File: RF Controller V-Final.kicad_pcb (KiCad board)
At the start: 2 copper layers, 132 x 67.5 mm, 37 parts, among them J3 BAT+, J4 BAT-, SW1 EG1218, U1 Teensy4.0, U7 Pitch/Roll, U9 Throttle/Yaw

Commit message: Modified traces
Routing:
- net /CSN: track 62.1 -> 62.7 mm
- net /MOSI: vias 2 -> 3
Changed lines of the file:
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@@
 	)
 	(segment
-		(start 136.82 102.18)
-		(end 114.03 102.18)
+		(start 136 103)
+		(end 114.85 103)
 		(width 0.2)
 		(layer "F.Cu")
@@
 	)
 	(segment
+		(start 114.85 103)
+		(end 112.93 101.08)
+		(width 0.2)
+		(layer "F.Cu")
+		(net "/CSN")
+	)
+	(segment
 		(start 138.5 100.5)
-		(end 136.82 102.18)
-		(width 0.2)
-		(layer "F.Cu")
-		(net "/CSN")
-	)
-	(segment
-		(start 114.03 102.18)
-		(end 112.93 101.08)
+		(end 136 103)
 		(width 0.2)
 		(layer "F.Cu")
@@
 	)
 	(segment
+		(start 135.5 102.4)
+		(end 116.79 102.4)
+		(width 0.2)
+		(layer "F.Cu")
+		(net "/MOSI")
+	)
+	(segment
 		(start 158.5 81.5)
 		(end 156.5 81.5)
@@
 		(net "/MOSI")
 	)
+	(segment
+		(start 116.79 102.4)
+		(end 115.47 101.08)
+		(width 0.2)
+		(layer "F.Cu")
+		(net "/MOSI")
+	)
 	(via
 		(at 158.534265 81.534265)
+		(size 0.6)
+		(drill 0.3)
+		(layers "F.Cu" "B.Cu")
+		(net "/MOSI")
+	)
+	(via
+		(at 135.5 102.4)
 		(size 0.6)
 		(drill 0.3)
@@
 	)
 	(segment
-		(start 135.5 102.5)
-		(end 116.89 102.5)
-		(width 0.2)
-		(layer "B.Cu")
-		(net "/MOSI")
-	)
-	(segment
 		(start 163.07 78.016346)
 		(end 159.552081 81.534265)
@@
 	)
 	(segment
-		(start 116.89 102.5)
-		(end 115.47 101.08)
-		(width 0.2)
-		(layer "B.Cu")
-		(net "/MOSI")
-	)
-	(segment
 		(start 156.5 81.5)
 		(end 135.5 102.5)
+		(width 0.2)
+		(layer "B.Cu")
+		(net "/MOSI")
+	)
+	(segment
+		(start 135.5 102.5)
+		(end 135.5 102.4)
 		(width 0.2)
 		(layer "B.Cu")
@@
 		(polygon
 			(pts
-				(xy 82 71) (xy 84.5 68) (xy 211 68) (xy 214 71) (xy 214 133) (xy 211.5 135.5) (xy 85 135.5) (xy 82 133)
+				(xy 82 70.5) (xy 84.5 68) (xy 211.5 68) (xy 214 71) (xy 214 133) (xy 211.5 135.5) (xy 84.5 135.5)
+				(xy 82 133)
 			)
 		)

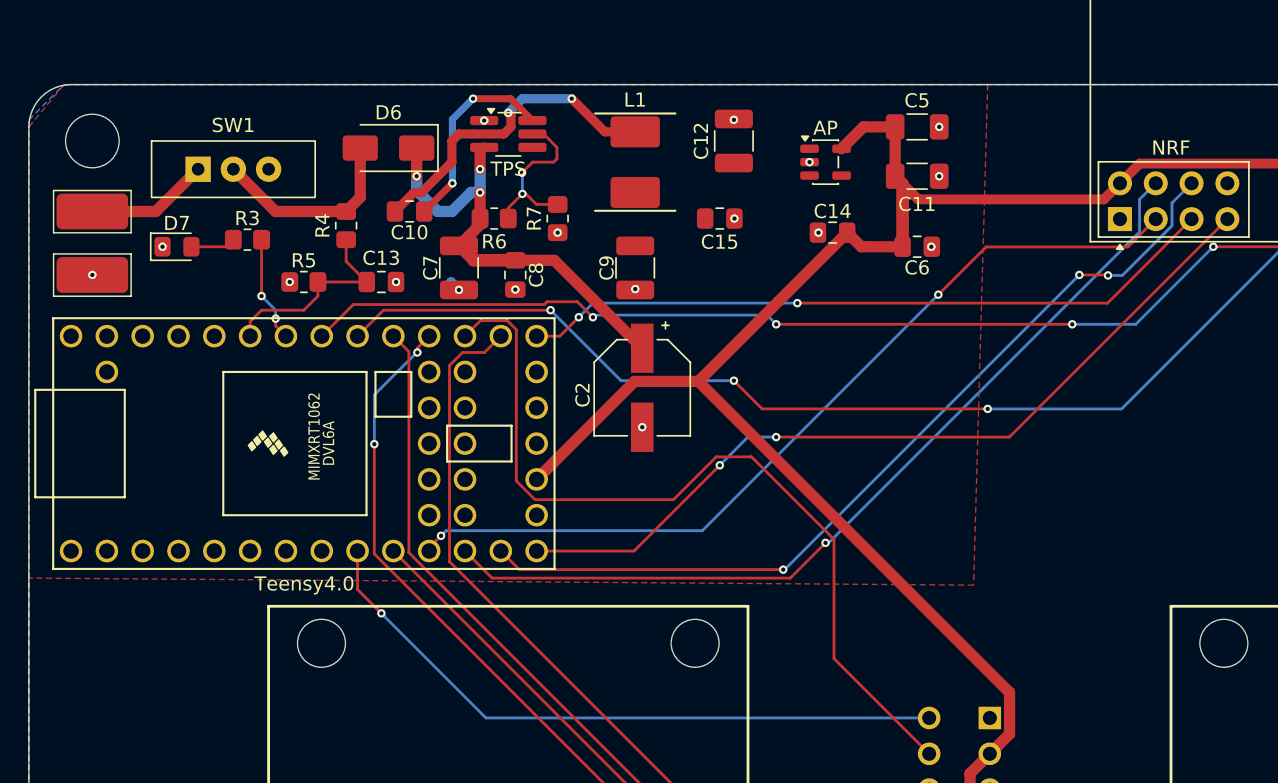
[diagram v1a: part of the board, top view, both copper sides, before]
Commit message: Modified 3.3V_OUT nets
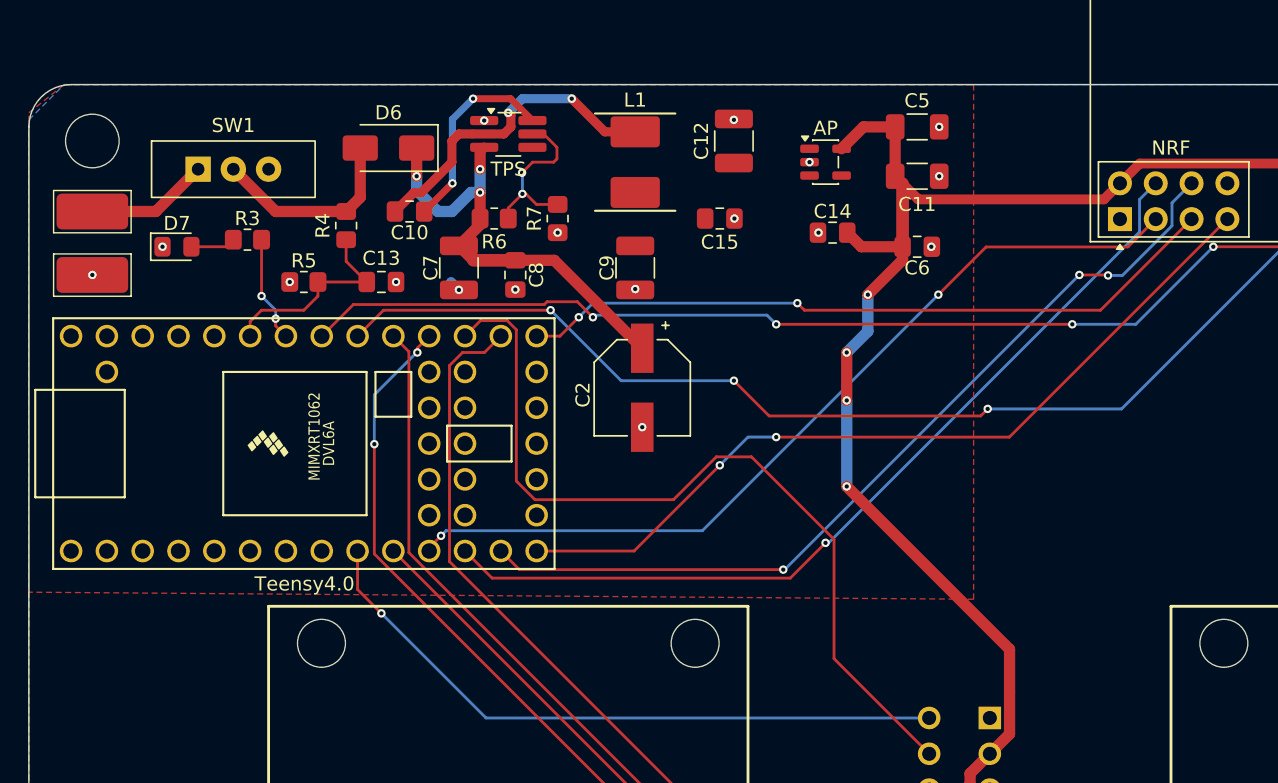
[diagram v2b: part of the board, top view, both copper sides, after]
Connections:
- U1 pad 16: /3.3V_OUT -> unconnected-(U1-3V3-Pad16)
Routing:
- net /3.3V_OUT: track 151.6 -> 129.2 mm, vias 0 -> 4
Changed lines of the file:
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@@
 			(layers "*.Cu" "*.Mask")
 			(remove_unused_layers no)
-			(net "/3.3V_OUT")
+			(net "unconnected-(U1-3V3-Pad16)")
 			(pinfunction "3V3_16")
-			(pintype "power_out")
+			(pintype "power_out+no_connect")
 		)
 		(pad "17" thru_hole circle
@@
 	)
 	(segment
+		(start 151.55 108.05)
+		(end 151.55 111.1125)
+		(width 0.8)
+		(layer "F.Cu")
+		(net "/3.3V_OUT")
+	)
+	(segment
 		(start 148.75 116.86)
 		(end 148.75 117.64)
@@
 	)
 	(segment
-		(start 129.4875 89.05)
-		(end 124.96 89.05)
+		(start 143.9625 80.4375)
+		(end 141.5 82.9)
 		(width 0.8)
 		(layer "F.Cu")
@@
 	)
 	(segment
-		(start 124.96 89.05)
-		(end 118.01 96)
+		(start 151.55 114.06)
+		(end 150.15 115.46)
 		(width 0.8)
 		(layer "F.Cu")
@@
 	)
 	(segment
-		(start 151.55 114.06)
-		(end 150.15 115.46)
+		(start 140 87)
+		(end 140 90.4)
 		(width 0.8)
 		(layer "F.Cu")
@@
 	)
 	(segment
-		(start 129.4875 89.05)
-		(end 151.55 111.1125)
+		(start 140 96.5)
+		(end 151.55 108.05)
+		(width 0.8)
+		(layer "F.Cu")
+		(net "/3.3V_OUT")
+	)
+	(segment
+		(start 143.9625 79.5)
+		(end 143.9625 80.4375)
 		(width 0.8)
 		(layer "F.Cu")
@@
 	)
 	(segment
-		(start 140.0375 78.5)
-		(end 129.4875 89.05)
-		(width 0.8)
-		(layer "F.Cu")
-		(net "/3.3V_OUT")
-	)
-	(segment
 		(start 171.6 73.6)
 		(end 174.5 76.5)
@@
 		(net "/3.3V_OUT")
 	)
+	(via
+		(at 140 87)
+		(size 0.6)
+		(drill 0.3)
+		(layers "F.Cu" "B.Cu")
+		(net "/3.3V_OUT")
+	)
+	(via
+		(at 140 90.4)
+		(size 0.6)
+		(drill 0.3)
+		(layers "F.Cu" "B.Cu")
+		(net "/3.3V_OUT")
+	)
+	(via
+		(at 140 96.5)
+		(size 0.6)
+		(drill 0.3)
+		(layers "F.Cu" "B.Cu")
+		(net "/3.3V_OUT")
+	)
+	(via
+		(at 141.5 82.9)
+		(size 0.6)
+		(drill 0.3)
+		(layers "F.Cu" "B.Cu")
+		(net "/3.3V_OUT")
+	)
+	(segment
+		(start 141.5 82.9)
+		(end 141.5 85.5)
+		(width 0.8)
+		(layer "B.Cu")
+		(net "/3.3V_OUT")
+	)
+	(segment
+		(start 141.5 85.5)
+		(end 140 87)
+		(width 0.8)
+		(layer "B.Cu")
+		(net "/3.3V_OUT")
+	)
+	(segment
+		(start 140 90.4)
+		(end 140 96.5)
+		(width 0.8)
+		(layer "B.Cu")
+		(net "/3.3V_OUT")
+	)
 	(segment
 		(start 125 82.5625)
@@
 	)
 	(segment
-		(start 158.5 83.5)
+		(start 137 84)
 		(end 136.5 83.5)
 		(width 0.2)
@@
 	(segment
 		(start 164.46 77.54)
-		(end 158.5 83.5)
+		(end 158 84)
+		(width 0.2)
+		(layer "F.Cu")
+		(net "/SCK")
+	)
+	(segment
+		(start 158 84)
+		(end 137 84)
 		(width 0.2)
 		(layer "F.Cu")
@@
 	)
 	(segment
+		(start 150 91)
+		(end 149.5 91.5)
+		(width 0.2)
+		(layer "F.Cu")
+		(net "/SDA")
+	)
+	(segment
 		(start 177 72.5)
 		(end 177.4 72.1)
@@
 	)
 	(segment
+		(start 134.5 91.5)
+		(end 132 89)
+		(width 0.2)
+		(layer "F.Cu")
+		(net "/SDA")
+	)
+	(segment
 		(start 191.81 69.5)
 		(end 196.11 73.8)
@@
 	)
 	(segment
-		(start 150 91)
-		(end 134 91)
+		(start 149.5 91.5)
+		(end 134.5 91.5)
 		(width 0.2)
 		(layer "F.Cu")
@@
 	)
 	(segment
-		(start 134 91)
-		(end 132 89)
-		(width 0.2)
-		(layer "F.Cu")
-		(net "/SDA")
-	)
-	(segment
 		(start 176.5 72.5)
 		(end 177 72.5)
@@
 		(polygon
 			(pts
-				(xy 82 71) (xy 84.5 68) (xy 150 68) (xy 149 103.5) (xy 82 103)
+				(xy 82 70) (xy 84.5 68) (xy 149 68) (xy 149 104.5) (xy 82 104)
 			)
 		)

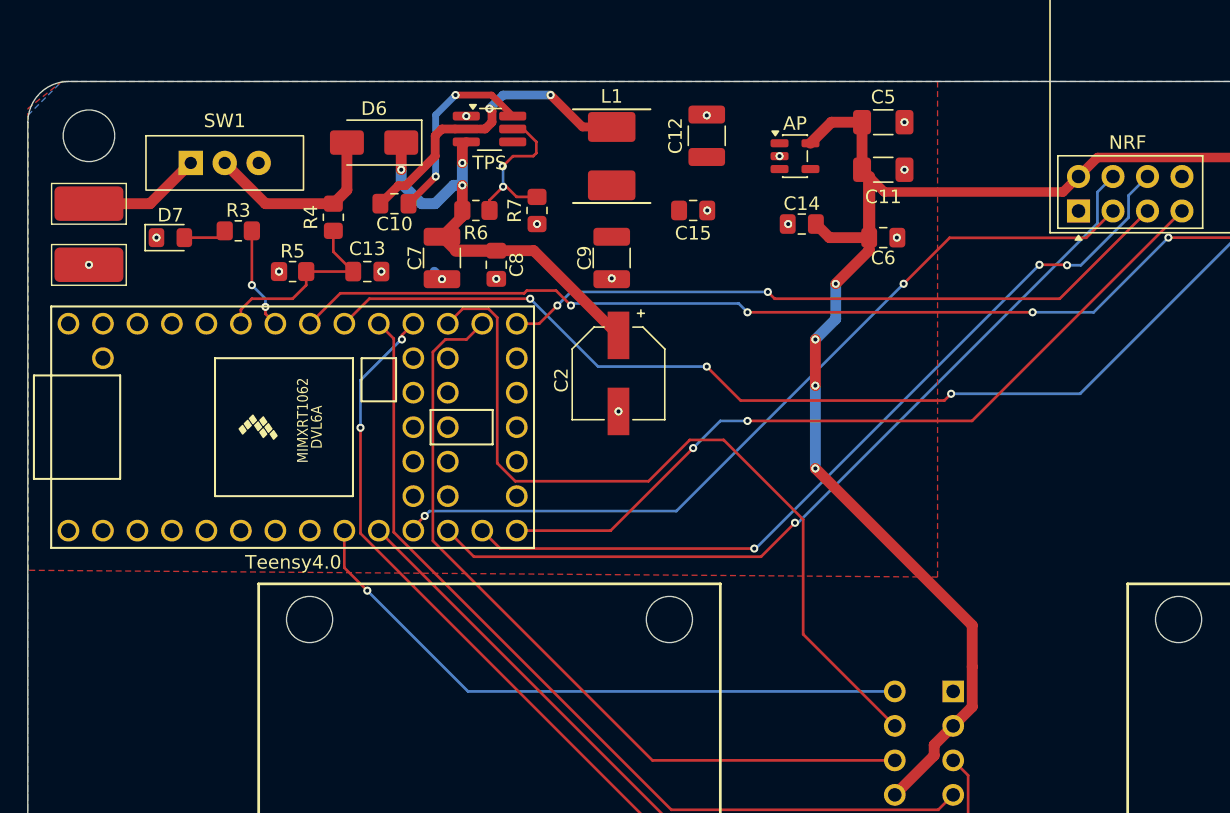
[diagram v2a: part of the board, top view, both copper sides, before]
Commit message: rewired joystick to 3v3
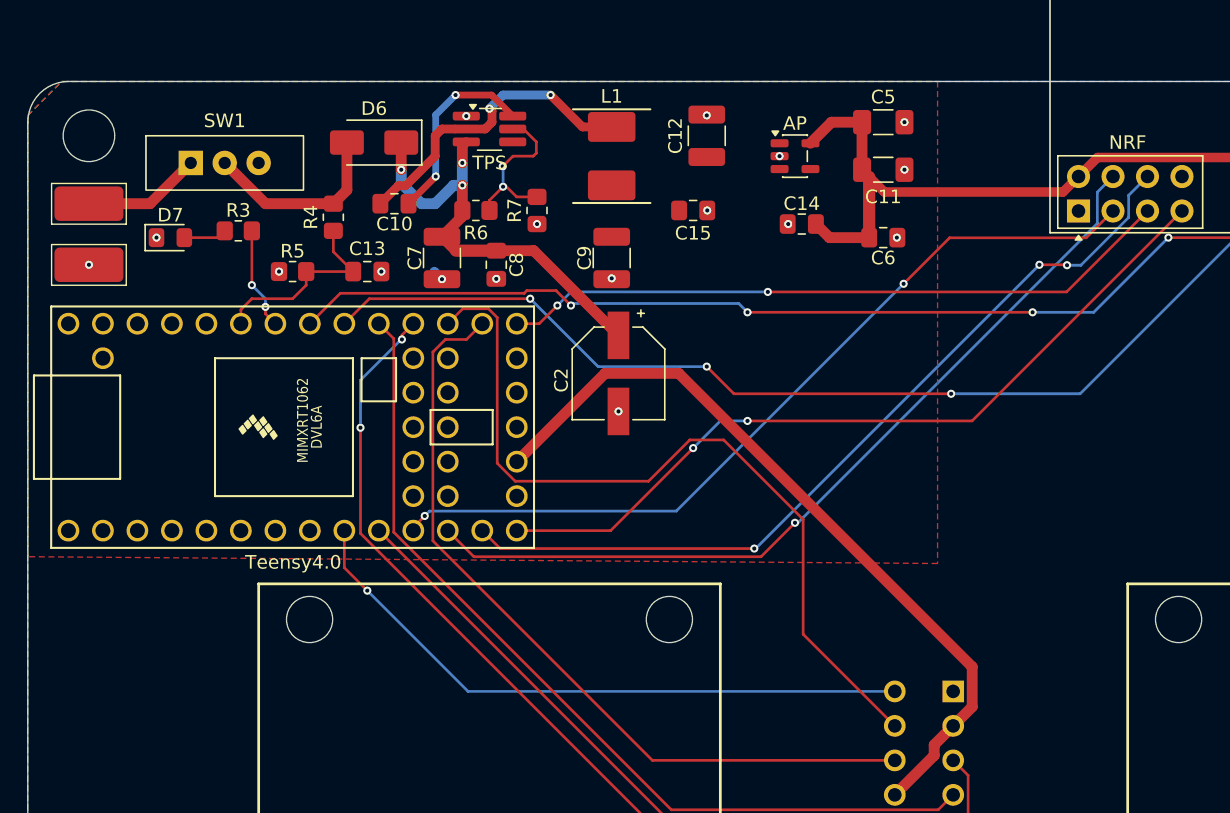
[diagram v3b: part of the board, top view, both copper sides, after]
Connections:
- U1 pad 16: unconnected-(U1-3V3-Pad16) -> /3v3
- U7 pad 2: /3.3V_OUT -> /3v3
- U9 pad 2: /3.3V_OUT -> /3v3
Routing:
- net /3v3: track 0.00 -> 57.0 mm
- net /3.3V_OUT: track 129.2 -> 79.4 mm, vias 4 -> 0
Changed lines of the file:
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@@
 			(layers "*.Cu" "*.Mask")
 			(remove_unused_layers no)
-			(net "unconnected-(U1-3V3-Pad16)")
+			(net "/3v3")
 			(pinfunction "3V3_16")
-			(pintype "power_out+no_connect")
+			(pintype "power_out")
 		)
 		(pad "17" thru_hole circle
@@
 			(layers "*.Cu" "*.Mask")
 			(remove_unused_layers no)
-			(net "/3.3V_OUT")
+			(net "/3v3")
 			(pinfunction "+5v_2")
 			(pintype "power_in")
@@
 			(layers "*.Cu" "*.Mask")
 			(remove_unused_layers no)
-			(net "/3.3V_OUT")
+			(net "/3v3")
 			(pinfunction "+5v_2")
 			(pintype "power_in")
@@
 	)
 	(segment
-		(start 151.55 108.05)
-		(end 151.55 111.1125)
-		(width 0.8)
-		(layer "F.Cu")
-		(net "/3.3V_OUT")
-	)
-	(segment
-		(start 148.75 116.86)
-		(end 148.75 117.64)
-		(width 0.8)
-		(layer "F.Cu")
-		(net "/3.3V_OUT")
-	)
-	(segment
-		(start 151.55 111.1125)
-		(end 151.55 114.06)
-		(width 0.8)
-		(layer "F.Cu")
-		(net "/3.3V_OUT")
-	)
-	(segment
 		(start 143.9625 79.5)
 		(end 143.9625 75.025)
@@
 	)
 	(segment
-		(start 143.9625 80.4375)
-		(end 141.5 82.9)
-		(width 0.8)
-		(layer "F.Cu")
-		(net "/3.3V_OUT")
-	)
-	(segment
 		(start 158.24 76.14)
 		(end 159.38 75)
@@
 	)
 	(segment
-		(start 150.15 115.46)
-		(end 148.75 116.86)
-		(width 0.8)
-		(layer "F.Cu")
-		(net "/3.3V_OUT")
-	)
-	(segment
-		(start 151.55 114.06)
-		(end 150.15 115.46)
-		(width 0.8)
-		(layer "F.Cu")
-		(net "/3.3V_OUT")
-	)
-	(segment
-		(start 140 87)
-		(end 140 90.4)
-		(width 0.8)
-		(layer "F.Cu")
-		(net "/3.3V_OUT")
-	)
-	(segment
 		(start 143.9625 75.025)
 		(end 143.4375 74.5)
@@
 	)
 	(segment
-		(start 140 96.5)
-		(end 151.55 108.05)
-		(width 0.8)
-		(layer "F.Cu")
-		(net "/3.3V_OUT")
-	)
-	(segment
-		(start 143.9625 79.5)
-		(end 143.9625 80.4375)
-		(width 0.8)
-		(layer "F.Cu")
-		(net "/3.3V_OUT")
-	)
-	(segment
 		(start 143.4375 71)
 		(end 141.1875 71)
@@
 	)
 	(segment
-		(start 148.75 117.64)
-		(end 145.85 120.54)
-		(width 0.8)
-		(layer "F.Cu")
-		(net "/3.3V_OUT")
-	)
-	(segment
 		(start 175.75 71.25)
 		(end 189.752792 71.25)
@@
 		(net "/3.3V_OUT")
 	)
-	(via
-		(at 140 87)
-		(size 0.6)
-		(drill 0.3)
-		(layers "F.Cu" "B.Cu")
-		(net "/3.3V_OUT")
-	)
-	(via
-		(at 140 90.4)
-		(size 0.6)
-		(drill 0.3)
-		(layers "F.Cu" "B.Cu")
-		(net "/3.3V_OUT")
-	)
-	(via
-		(at 140 96.5)
-		(size 0.6)
-		(drill 0.3)
-		(layers "F.Cu" "B.Cu")
-		(net "/3.3V_OUT")
-	)
-	(via
-		(at 141.5 82.9)
-		(size 0.6)
-		(drill 0.3)
-		(layers "F.Cu" "B.Cu")
-		(net "/3.3V_OUT")
-	)
-	(segment
-		(start 141.5 82.9)
-		(end 141.5 85.5)
-		(width 0.8)
-		(layer "B.Cu")
-		(net "/3.3V_OUT")
-	)
-	(segment
-		(start 141.5 85.5)
-		(end 140 87)
-		(width 0.8)
-		(layer "B.Cu")
-		(net "/3.3V_OUT")
-	)
-	(segment
-		(start 140 90.4)
-		(end 140 96.5)
-		(width 0.8)
-		(layer "B.Cu")
-		(net "/3.3V_OUT")
-	)
 	(segment
 		(start 125 82.5625)
@@
 	)
 	(segment
-		(start 137 84)
+		(start 158.5 83.5)
 		(end 136.5 83.5)
 		(width 0.2)
@@
 	(segment
 		(start 164.46 77.54)
-		(end 158 84)
-		(width 0.2)
-		(layer "F.Cu")
-		(net "/SCK")
-	)
-	(segment
-		(start 158 84)
-		(end 137 84)
+		(end 158.5 83.5)
 		(width 0.2)
 		(layer "F.Cu")
@@
 	)
 	(segment
-		(start 150 91)
-		(end 149.5 91.5)
-		(width 0.2)
-		(layer "F.Cu")
-		(net "/SDA")
-	)
-	(segment
 		(start 177 72.5)
 		(end 177.4 72.1)
@@
 	)
 	(segment
-		(start 134.5 91.5)
-		(end 132 89)
-		(width 0.2)
-		(layer "F.Cu")
-		(net "/SDA")
-	)
-	(segment
 		(start 191.81 69.5)
 		(end 196.11 73.8)
@@
 	)
 	(segment
-		(start 149.5 91.5)
-		(end 134.5 91.5)
+		(start 150 91)
+		(end 134 91)
 		(width 0.2)
 		(layer "F.Cu")
@@
 	)
 	(segment
+		(start 134 91)
+		(end 132 89)
+		(width 0.2)
+		(layer "F.Cu")
+		(net "/SDA")
+	)
+	(segment
 		(start 176.5 72.5)
 		(end 177 72.5)
@@
 		(net "/VBAT")
 	)
+	(segment
+		(start 148.75 116.86)
+		(end 148.75 117.64)
+		(width 0.8)
+		(layer "F.Cu")
+		(net "/3v3")
+	)
+	(segment
+		(start 150.15 115.46)
+		(end 148.75 116.86)
+		(width 0.8)
+		(layer "F.Cu")
+		(net "/3v3")
+	)
+	(segment
+		(start 151.55 111.1125)
+		(end 129.9375 89.5)
+		(width 0.8)
+		(layer "F.Cu")
+		(net "/3v3")
+	)
+	(segment
+		(start 124.51 89.5)
+		(end 118.01 96)
+		(width 0.8)
+		(layer "F.Cu")
+		(net "/3v3")
+	)
+	(segment
+		(start 148.75 117.64)
+		(end 145.85 120.54)
+		(width 0.8)
+		(layer "F.Cu")
+		(net "/3v3")
+	)
+	(segment
+		(start 150.15 115.46)
+		(end 151.55 114.06)
+		(width 0.8)
+		(layer "F.Cu")
+		(net "/3v3")
+	)
+	(segment
+		(start 129.9375 89.5)
+		(end 124.51 89.5)
+		(width 0.8)
+		(layer "F.Cu")
+		(net "/3v3")
+	)
+	(segment
+		(start 151.55 114.06)
+		(end 151.55 111.1125)
+		(width 0.8)
+		(layer "F.Cu")
+		(net "/3v3")
+	)
 	(zone
 		(net "/5V_IN")
@@
 		(polygon
 			(pts
-				(xy 82 70) (xy 84.5 68) (xy 149 68) (xy 149 104.5) (xy 82 104)
+				(xy 82 70.5) (xy 84.5 68) (xy 149 68) (xy 149 103.5) (xy 82 103)
 			)
 		)
